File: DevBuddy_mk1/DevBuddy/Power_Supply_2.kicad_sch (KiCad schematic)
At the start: 0 parts

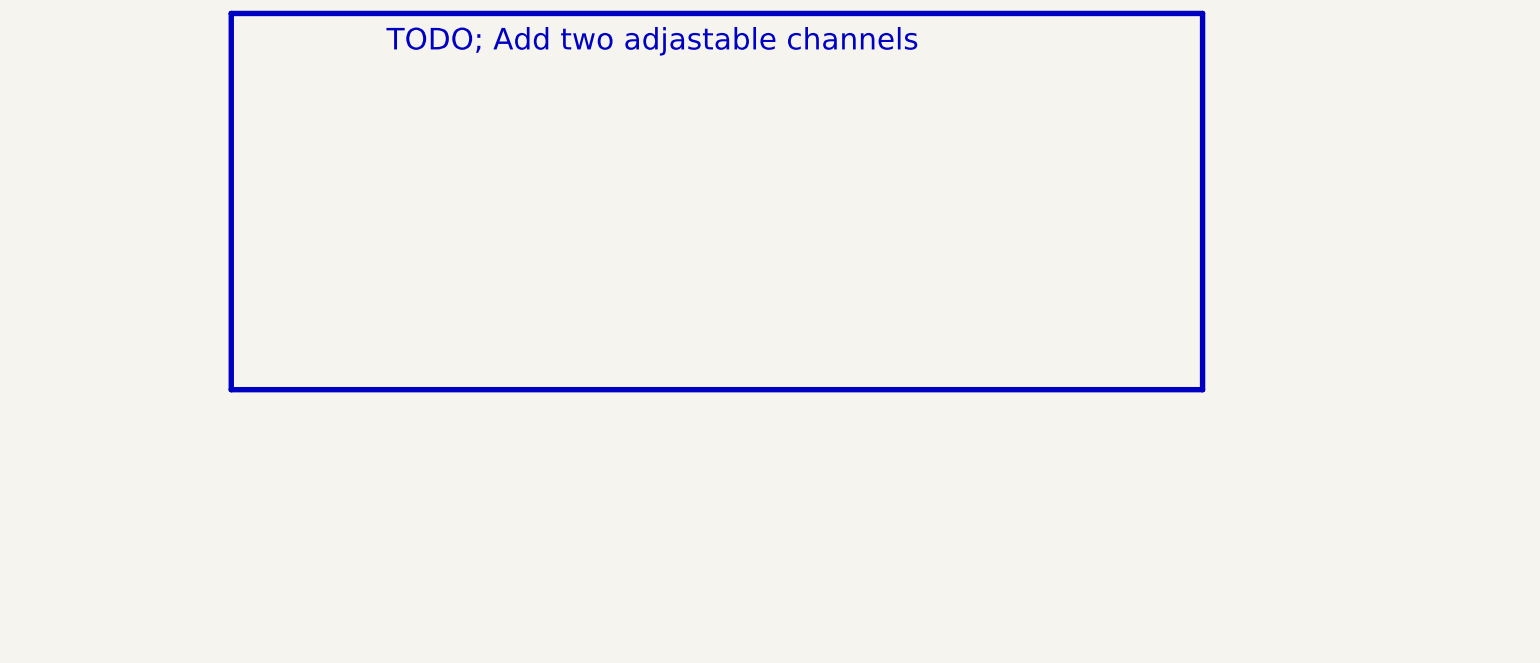
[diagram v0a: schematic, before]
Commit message: Changes in Variable buck - Hardware
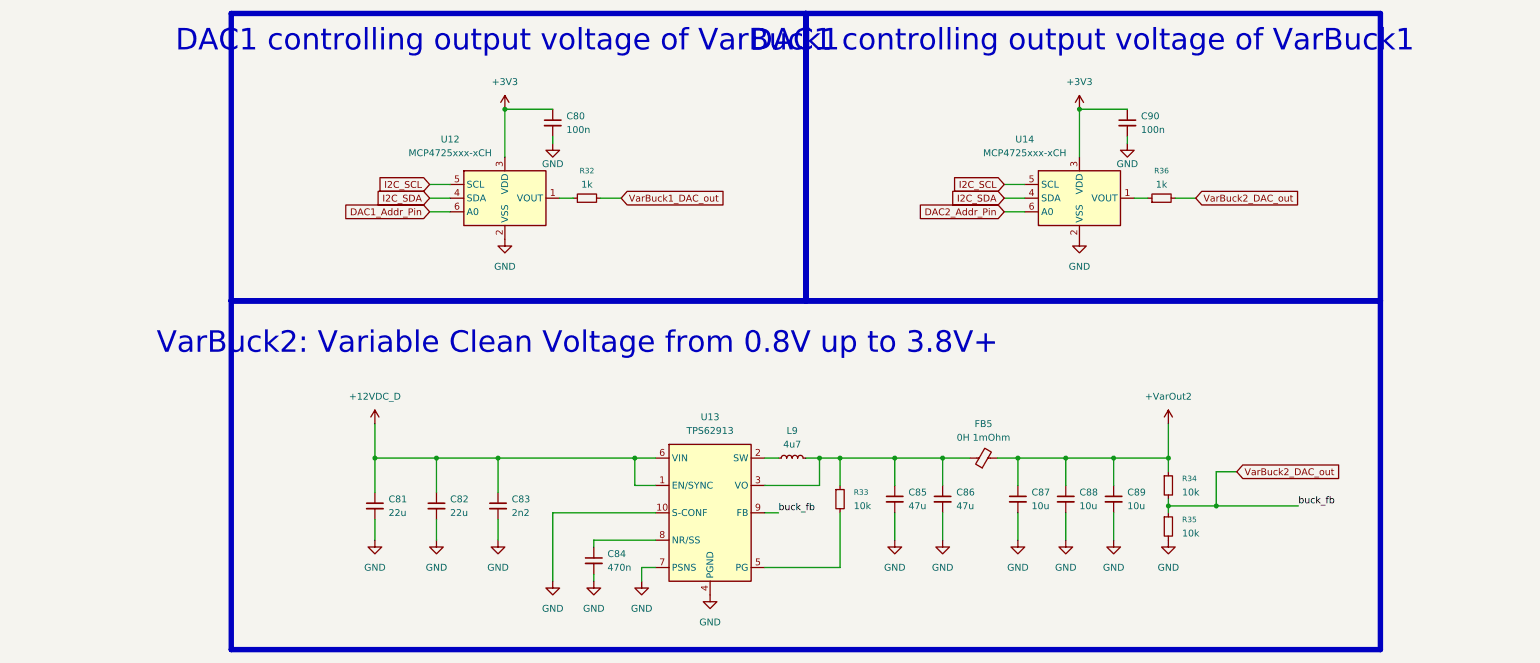
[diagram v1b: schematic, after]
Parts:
- added C80, C90: 100n, Capacitor_SMD:C_0402_1005Metric, symbol Device:C_Small
- added C81, C82: 22u, Capacitor_SMD:C_0805_2012Metric, symbol Device:C_Small
- added C83: 2n2, Capacitor_SMD:C_0402_1005Metric, symbol Device:C_Small
- added C84: 470n, Capacitor_SMD:C_0402_1005Metric, symbol Device:C_Small
- added C85, C86: 47u, Capacitor_SMD:C_0805_2012Metric, symbol Device:C_Small
- added C87, C88, C89: 10u, Capacitor_SMD:C_0805_2012Metric, symbol Device:C_Small
- added FB5: 0H 1mOhm, symbol Device:FerriteBead_Small
- added L9: 4u7, Inductor_SMD:L_Coilcraft_XAL6060-XXX, symbol Device:L_Small
- added R32, R36: 1k, Resistor_SMD:R_0402_1005Metric, symbol Device:R_Small
- added R33, R34, R35: 10k, Resistor_SMD:R_0402_1005Metric, symbol Device:R_Small
- added U12, U14: MCP4725xxx-xCH, Package_TO_SOT_SMD:SOT-23-6, symbol Analog_DAC:MCP4725xxx-xCH
- added U13: TPS62913, Package_DFN_QFN:Texas_RPU0010A_VQFN-HR-10_2x2mm_P0.5mm, symbol Regulator_Switching:TPS62913
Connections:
- new net: C85.1, C86.1, FB5.1, L9.2, R33.1, U13.3 (VO)
- new net: R33.2, U13.5 (PG)
- new net: R36.1, U14.1 (VOUT)
- new net: L9.1, U13.2 (SW)
- new net: C84.1, U13.8 (NR/SS)
- new net: R32.1, U12.1 (VOUT)
- new net +12VDC_D: C81.1, C82.1, C83.1, U13.1 (EN/SYNC), U13.6 (VIN)
- new net +3V3: C80.1, C90.1, U12.3 (VDD), U14.3 (VDD)
- new net +VarOut2: C87.1, C88.1, C89.1, FB5.2, R34.1
- new net DAC1_Addr_Pin: U12.6 (A0)
- new net DAC2_Addr_Pin: U14.6 (A0)
- new net GND: C80.2, C81.2, C82.2, C83.2, C84.2, C85.2, C86.2, C87.2, C88.2, C89.2, C90.2, R35.2, U12.2 (VSS), U13.10 (S-CONF), U13.4 (PGND), U13.7 (PSNS), U14.2 (VSS)
- new net I2C_SCL: U12.5 (SCL), U14.5 (SCL)
- new net I2C_SDA: U12.4 (SDA), U14.4 (SDA)
- new net VarBuck1_DAC_out: R32.2
- new net VarBuck2_DAC_out: R34.2, R35.1, R36.2, U13.9 (FB)
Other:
- note added: "DAC1 controlling output voltage of VarBuck1"
- note added: "VarBuck2: Variable Clean Voltage from 0.8V up to 3.8V+"
- note removed: "TODO; Add two adjastable channels"

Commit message: Added variable voltage channels/ PCB
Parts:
- removed C81: 22u, Capacitor_SMD:C_0805_2012Metric, symbol Device:C_Small
- removed FB5: 0H 1mOhm, symbol Device:FerriteBead_Small
- removed U13: TPS62913, Package_DFN_QFN:Texas_RPU0010A_VQFN-HR-10_2x2mm_P0.5mm, symbol Regulator_Switching:TPS62913
- added C100, C93: 39u, Capacitor_SMD:CP_Elec_5x5.9, symbol Device:C_Polarized_Small
- added C101, C102, C56: 1u, Capacitor_SMD:C_0402_1005Metric, symbol Device:C_Small
- added C45, C81: 22u, Capacitor_Tantalum_SMD:CP_EIA-7343-31_Kemet-D, symbol Device:C_Polarized_Small
- added C53: 10u, Capacitor_SMD:C_1210_3225Metric, symbol Device:C_Small
- added C58: 10n, Capacitor_SMD:C_0402_1005Metric, symbol Device:C_Small
- added C63: 4u7, Capacitor_SMD:C_0603_1608Metric, symbol Device:C_Small
- added C66, C94: 100n, Capacitor_SMD:C_0603_1608Metric, symbol Device:C_Small
- added C69: 560p, Capacitor_SMD:C_0402_1005Metric, symbol Device:C_Small
- added C71: 2.4p, Capacitor_SMD:C_0402_1005Metric, symbol Device:C_Small
- added C73, C91: 1u, Capacitor_SMD:C_0603_1608Metric, symbol Device:C_Small
- added C92, C95, C96, C97, C98, C99: 10u, Capacitor_SMD:C_0805_2012Metric, symbol Device:C_Small
- added L6: 4.7uH - 10mOhm - 7.8A, Inductor_SMD:L_Bourns-SRN8040_8x8.15mm, symbol Device:L_Small
- added R23: 715k, Resistor_SMD:R_0402_1005Metric, symbol Device:R_Small
- added R28, R47, R48: 100k, Resistor_SMD:R_0402_1005Metric, symbol Device:R_Small
- added R29: 8k25, Resistor_SMD:R_0402_1005Metric, symbol Device:R_Small
- added R37, R38: 10k, Resistor_SMD:R_0402_1005Metric, symbol Device:R_Small
- added R41, R42: 105k, Resistor_SMD:R_0402_1005Metric, symbol Device:R_Small
- added R43, R45: 10m, Resistor_SMD:R_1206_3216Metric, symbol Device:R_Small
- added R44, R46: 0R, Resistor_SMD:R_0402_1005Metric, symbol Device:R_Small
- added R49, R50, R51, R52: 10R, Resistor_SMD:R_0402_1005Metric, symbol Device:R_Small
- added U13, U9: TPS55289RYQR, TPS55289RYQR:RYQ0021A-MFG, symbol TPS55289RYQR:TPS55289RYQR
- C82: value 22u -> 10u; footprint Capacitor_SMD:C_0805_2012Metric -> Capacitor_SMD:C_1210_3225Metric
- C83: value 2n2 -> 1u
- C84: value 470n -> 4u7; footprint Capacitor_SMD:C_0402_1005Metric -> Capacitor_SMD:C_0603_1608Metric
- C85: value 47u -> 10n; footprint Capacitor_SMD:C_0805_2012Metric -> Capacitor_SMD:C_0402_1005Metric
- C86: value 47u -> 560p; footprint Capacitor_SMD:C_0805_2012Metric -> Capacitor_SMD:C_0402_1005Metric
- C87: value 10u -> 2.4p; footprint Capacitor_SMD:C_0805_2012Metric -> Capacitor_SMD:C_0402_1005Metric
- C88, C89: value 10u -> 100n; footprint Capacitor_SMD:C_0805_2012Metric -> Capacitor_SMD:C_0603_1608Metric
- L9: value 4u7 -> 4.7uH - 10mOhm - 7.8A; footprint Inductor_SMD:L_Coilcraft_XAL6060-XXX -> Inductor_SMD:L_Bourns-SRN8040_8x8.15mm
- R33: value 10k -> 715k
- R34: value 10k -> 100k
- R35: value 10k -> 8k25
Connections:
- net +12VDC_D: now also R33.1, C45.1, C53.1, C56.1, C81.1, R23.1, U13.7 (VIN), U9.7 (VIN)
- net +3V3: now also R37.1
- net GND: now also R34.2, C100.2, C45.2, C53.2, C56.2, C63.2, C73.2, C81.2, C91.2, C92.2, C93.2, C95.2, C96.2, C97.2, C98.2, C99.2, R28.2, R38.1, R44.1, R46.1, U13.9 (PGND), U9.9 (PGND); no longer C85.2, C86.2, C87.2, C88.2, C89.2, R35.2
- net I2C_SCL: now also U13.3 (SCL), U9.3 (SCL)
- net I2C_SDA: now also U13.4 (SDA), U9.4 (SDA)
- net VarBuck2_DAC_out: no longer R34.2, R35.1
- net at R33.2: now also R34.1, U13.1 (EN_UVLO)
- net at L9.1: now also C88.1, U13.8 (SW1)
- net VCC_buck_2: now reaches C84.1
- net VCC_buck_2: now also R48.2, U13.18 (VCC), U13.21 (EXTVCC)
- removed net +VarOut2: C87.1, C88.1, C89.1, R34.1
- net DAC1_Addr_Pin: no longer names the net of U12.6 (A0)
- net DAC1_Addr_Pin: now also R38.2
- net DAC2_Addr_Pin: no longer names the net of U14.6 (A0)
- net DAC2_Addr_Pin: now also R37.2
- new net: R23.2, R28.1, U9.1 (EN_UVLO)
- new net: C101.2, R49.1, U9.13 (ISN)
- new net: C100.1, C73.1, C95.1, C96.1, C99.1, R45.1, R50.2, U9.11 (VOUT)
- new net: C91.1, C92.1, C93.1, C97.1, C98.1, R43.1, R51.2, U13.11 (VOUT)
- new net: R48.1, U13.14 (FB_INT_N)
- new net: C89.1, L9.2, U13.10 (SW2)
- new net: C89.2, U13.19 (BOOT2)
- new net: C66.1, L6.1, U9.8 (SW1)
- new net: C94.1, L6.2, U9.10 (SW2)
- new net: C69.2, R42.1
- new net: C58.1, U9.5 (DITH_SYNC)
- new net: R35.1, U13.6 (FSW)
- new net: C86.2, R41.1
- new net: C69.1, C71.1, U9.15 (COMP)
- new net: C88.2, U13.20 (BOOT1)
- new net: C102.1, R51.1, U13.12 (ISP)
- new net: C102.2, R52.1, U13.13 (ISN)
- new net: C66.2, U9.20 (BOOT1)
- new net: R47.1, U9.14 (FB_INT_N)
- new net: C101.1, R50.1, U9.12 (ISP)
- new net: R29.1, U9.6 (FSW)
- new net: C85.1, U13.5 (DITH_SYNC)
- new net: C86.1, C87.1, U13.15 (COMP)
- new net: C94.2, U9.19 (BOOT2)
- new net +Var_V_1: R45.2, R49.2
- new net +Var_V_2: R43.2, R52.2
- new net AGND: C58.2, C71.2, C85.2, C87.2, R29.2, R35.2, R41.2, R42.2, R44.2, R46.2, U13.17 (AGND), U13.2 (MODE), U9.17 (AGND)
- new net VCC_buck: C63.1, R47.2, U9.18 (VCC), U9.2 (MODE), U9.21 (EXTVCC)
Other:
- note added: "DAC1 controlling output voltage 1"
- note added: "DAC2 controlling output voltage 2"
- note added: "VarBuck1: Variable Clean Voltage from 0.8V up to 3.8V+ | Addr 75h"
- note added: "VarBuck2: Variable Clean Voltage from 0.8V up to 3.8V+ | Addr 74h"
- note removed: "DAC1 controlling output voltage of VarBuck1"
- note removed: "VarBuck2: Variable Clean Voltage from 0.8V up to 3.8V+"

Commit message: Heavy additions to schematic
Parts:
- added R82, R83: 10mOhm, Resistor_SMD:R_1210_3225Metric, symbol Device:R
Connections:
- net +Var_V_1: now also R83.2; no longer R45.2, R49.2
- net +Var_V_2: now also R82.2; no longer R43.2, R52.2
- net Var_V1_CurSense_Hi: now reaches C100.1, C73.1, C95.1, C96.1, C99.1, R45.1, R50.2, U9.11 (VOUT)
- net Var_V2_CurSense_Hi: now reaches C91.1, C92.1, C93.1, C97.1, C98.1, R43.1, R51.2, U13.11 (VOUT)
- new net: R45.2, R49.2, R83.1
- new net: R43.2, R52.2, R82.1
